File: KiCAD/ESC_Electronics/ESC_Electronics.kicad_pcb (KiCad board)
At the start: 2 copper layers, 149.5 x 74.5 mm, 70 parts, among them J1 -1000VDC, J2 Test Input, J3 CA probe, J4 DC Power, J5 Output, J6 Barrel_Jack, J7 -6V, J8 +6V, J9 Batt probe, Q1 MMBT3906, Q2 MMBT3904, U1 CR110, U2 SiPhotodiode, U3 TL072, U4 LM317, U5 TLE2426xP

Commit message: published as V2 on OSHPark
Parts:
- removed D3, D4: RB751V-40, Diode_SMD:D_SOD-323_HandSoldering
- removed D5, D6: MM3Z7V5T1G, Diode_SMD:D_SOD-323_HandSoldering
- removed Q1: MMBT3906, Package_TO_SOT_SMD:SOT-23
- removed Q2: MMBT3904, Package_TO_SOT_SMD:SOT-23
- removed R15: 220, Resistor_SMD:R_0805_2012Metric_Pad1.20x1.40mm_HandSolder
- removed R16, R17: 1k, Resistor_SMD:R_0805_2012Metric_Pad1.20x1.40mm_HandSolder
- removed R18, R19: 20, Resistor_SMD:R_1206_3216Metric_Pad1.30x1.75mm_HandSolder
- removed R20: 10k, Resistor_THT:R_Axial_DIN0207_L6.3mm_D2.5mm_P10.16mm_Horizontal
- removed R5: 100M, Resistor_THT:R_Axial_DIN0207_L6.3mm_D2.5mm_P10.16mm_Horizontal
- added C14: 0.33uF, Capacitor_SMD:C_0805_2012Metric_Pad1.18x1.45mm_HandSolder, F.Cu at (106.0, 106.5)
- added C15: 100nF, Capacitor_SMD:C_0805_2012Metric_Pad1.18x1.45mm_HandSolder, F.Cu at (100.7, 124.9)
- added C16: 100nF, Capacitor_SMD:C_0805_2012Metric_Pad1.18x1.45mm_HandSolder, F.Cu at (100.7, 119.8)
- added C17: 0.1uF, Capacitor_SMD:C_0805_2012Metric_Pad1.18x1.45mm_HandSolder, F.Cu at (70.5, 101.5)
- added C18: 0.1uF, Capacitor_SMD:C_0805_2012Metric_Pad1.18x1.45mm_HandSolder, F.Cu at (89.2, 101.5)
- added FB1: FerriteBead_Small, Inductor_SMD:L_1206_3216Metric_Pad1.22x1.90mm_HandSolder, F.Cu at (92.0, 86.8)
- added FB2: FerriteBead_Small, Inductor_SMD:L_1206_3216Metric_Pad1.22x1.90mm_HandSolder, F.Cu at (92.0, 80.6)
- added J10: RV Prob, Connector_PinHeader_2.54mm:PinHeader_1x02_P2.54mm_Vertical, F.Cu at (64.0, 96.0)
- added RV1: 10k, Potentiometer_THT:Potentiometer_Bourns_3266W_Vertical, F.Cu at (59.4, 88.3)
- added U6: UA79M08, Package_TO_SOT_SMD:TO-252-3_TabPin2, F.Cu at (97.6, 105.2)
- added U7: TLE2426xP, Package_SO:SOIC-8_3.9x4.9mm_P1.27mm, F.Cu at (106.6, 122.1)
- C10: value 1uF -> 0.1uF
- C11, C12: value 10uF -> 1uF
- C13: value 0.1uF -> 0.33uF
- C3: footprint Capacitor_THT:C_Disc_D10.5mm_W5.0mm_P7.50mm -> Capacitor_THT:C_Disc_D10.5mm_W5.0mm_P10.00mm
- C5: value 1nF -> 1pF; footprint Capacitor_THT:C_Disc_D10.5mm_W5.0mm_P7.50mm -> Capacitor_THT:C_Disc_D7.5mm_W5.0mm_P5.00mm
- C6: value 1pF -> 4700pF; footprint Capacitor_THT:C_Disc_D7.5mm_W5.0mm_P5.00mm -> Capacitor_THT:C_Disc_D12.5mm_W5.0mm_P10.00mm
- C7: value 4700pF -> 1nF; footprint Capacitor_THT:C_Disc_D14.5mm_W5.0mm_P7.50mm -> Capacitor_THT:C_Disc_D10.5mm_W5.0mm_P10.00mm
- C8: value 1uF -> open
- J1: value -1000VDC -> Batt probe; footprint ESC_Electronics_Library:MHV Wire Conn -> Connector_PinHeader_2.54mm:PinHeader_1x02_P2.54mm_Vertical
- J2: value Test Input -> CA probe; footprint Connector_Coaxial:BNC_Amphenol_B6252HB-NPP3G-50_Horizontal -> Connector_PinHeader_2.54mm:PinHeader_1x02_P2.54mm_Vertical
- J3: value CA probe -> Test Input; footprint Connector_PinHeader_2.54mm:PinHeader_1x02_P2.54mm_Vertical -> Connector_Coaxial:BNC_Amphenol_B6252HB-NPP3G-50_Horizontal
- J4: value DC Power -> -1000VDC; footprint TerminalBlock_4Ucon:TerminalBlock_4Ucon_1x03_P3.50mm_Vertical -> ESC_Electronics_Library:MHV Wire Conn
- J6: footprint Connector_Wire:SolderWire-0.5sqmm_1x02_P4.6mm_D0.9mm_OD2.1mm -> Connector_PinHeader_2.54mm:PinHeader_1x02_P2.54mm_Vertical
- J7: value -6V -> DC Power; footprint Connector_PinHeader_2.54mm:PinHeader_1x02_P2.54mm_Vertical -> Connector_PinHeader_2.54mm:PinHeader_1x03_P2.54mm_Vertical
- J8: value +6V -> -8V
- J9: value Batt probe -> +8V
- R10: value 47 -> 750
- R11: value 1k -> 20k; footprint Resistor_THT:R_Axial_DIN0207_L6.3mm_D2.5mm_P10.16mm_Horizontal -> Resistor_SMD:R_0805_2012Metric_Pad1.20x1.40mm_HandSolder
- R12: value 10k -> 4.7; footprint Resistor_THT:R_Axial_DIN0207_L6.3mm_D2.5mm_P10.16mm_Horizontal -> Resistor_SMD:R_2512_6332Metric_Pad1.40x3.35mm_HandSolder
- R13: value 4.7 -> 7k; footprint Resistor_SMD:R_2512_6332Metric_Pad1.40x3.35mm_HandSolder -> Resistor_SMD:R_0805_2012Metric_Pad1.20x1.40mm_HandSolder
- R14: value 2.94k -> 470
- R2: value 4.7 -> 10M; footprint Resistor_SMD:R_2512_6332Metric_Pad1.40x3.35mm_HandSolder -> Resistor_THT:R_Axial_DIN0207_L6.3mm_D2.5mm_P15.24mm_Horizontal
- R3: footprint Resistor_THT:R_Axial_DIN0207_L6.3mm_D2.5mm_P10.16mm_Horizontal -> Resistor_THT:R_Axial_DIN0207_L6.3mm_D2.5mm_P15.24mm_Horizontal
- R4: value 10M -> 100M; footprint Resistor_THT:R_Axial_DIN0207_L6.3mm_D2.5mm_P10.16mm_Horizontal -> Resistor_THT:R_Axial_DIN0207_L6.3mm_D2.5mm_P15.24mm_Horizontal
- R6: value 0 -> 10M; footprint Resistor_THT:R_Axial_DIN0207_L6.3mm_D2.5mm_P10.16mm_Horizontal -> Resistor_THT:R_Axial_DIN0207_L6.3mm_D2.5mm_P15.24mm_Horizontal
- R7: value 4.7 -> 47; footprint Resistor_SMD:R_2512_6332Metric_Pad1.40x3.35mm_HandSolder -> Resistor_SMD:R_0805_2012Metric_Pad1.20x1.40mm_HandSolder
- R8: value 10M -> open; footprint Resistor_THT:R_Axial_DIN0207_L6.3mm_D2.5mm_P10.16mm_Horizontal -> Resistor_THT:R_Axial_DIN0207_L6.3mm_D2.5mm_P15.24mm_Horizontal
- R9: value open -> 0; footprint Resistor_THT:R_Axial_DIN0207_L6.3mm_D2.5mm_P7.62mm_Horizontal -> Resistor_SMD:R_1206_3216Metric_Pad1.30x1.75mm_HandSolder
- U3: value TL072 -> TL051CP
- U4: value LM317 -> LM317L; footprint Package_TO_SOT_THT:TO-220-3_Horizontal_TabDown -> Package_TO_SOT_SMD:SOT-89-3_Handsoldering
- U5: value TLE2426xP -> UA78M08; footprint Package_TO_SOT_THT:TO-92L_Inline_Wide -> Package_TO_SOT_SMD:SOT-223-3_TabPin2
- moved J4 111.6 mm to (164.8, 63.8), turned to 0 degrees
- moved R9 102.6 mm to (84.7, 90.8), turned to 180 degrees
- moved C6 73.1 mm to (137.8, 71.8), turned to 180 degrees
- moved J9 70.2 mm to (79.0, 97.8)
- moved R2 66.0 mm to (138.8, 111.4)
- moved J1 62.8 mm to (127.0, 108.8), turned to 180 degrees
- moved C5 60.8 mm to (119.0, 64.5), turned to 90 degrees
- moved C7 55.0 mm to (188.5, 61.8), turned to -90 degrees
- moved J5 46.5 mm to (60.7, 65.2)
- moved R7 42.6 mm to (113.5, 63.8)
- moved R12 40.7 mm to (78.0, 124.8), turned to 180 degrees
- moved C9 40.6 mm to (70.6, 75.2), turned to 90 degrees
- moved C10 37.8 mm to (54.8, 82.8), turned to 90 degrees
- moved C2 37.8 mm to (90.8, 66.2), turned to 90 degrees
- moved R4 35.8 mm to (148.9, 72.0), turned to 0 degrees
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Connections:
- C1 pad 1: +6VDC -> Net-(C1-Pad1)
- C10 pad 1: Net-(C10-Pad1) -> +8VDC
- C10 pad 2: Net-(C10-Pad2) -> GND
- C11 pad 2: GND -> Net-(C11-Pad2)
- C12 pad 2: GND -> Net-(C11-Pad2)
- C13 pad 1: -6VDC -> Net-(C13-Pad1)
- C3 pad 2: Net-(C3-Pad2) -> Net-(R2-Pad2)
- C4 pad 1: -6VDC -> Net-(C4-Pad1)
- C5 pad 1: GND -> Net-(C2-Pad1)
- C5 pad 2: Net-(R5-Pad2) -> Net-(C5-Pad2)
- C6 pad 1: Net-(C2-Pad1) -> Net-(BT1-Pad2)
- C6 pad 2: Net-(C6-Pad2) -> GND
- C7 pad 1: Net-(BT1-Pad2) -> GND
- C7 pad 2: GND -> Net-(C7-Pad2)
- C8 pad 2: Net-(C10-Pad2) -> GND
- C9 pad 1: +6VDC -> -8VDC
- D1 pad 1: Net-(D1-Pad1) -> Net-(C13-Pad1)
- D1 pad 2: Net-(D1-Pad2) -> Net-(C12-Pad1)
- D2 pad 1: Net-(D2-Pad1) -> Net-(C11-Pad2)
- D2 pad 2: Net-(D2-Pad2) -> Net-(C14-Pad1)
- J1 pad 1: Net-(J1-Pad1) -> Net-(BT6-Pad1)
- J1 pad 2: GND -> Net-(BT1-Pad2)
- J2 pad 1: Net-(C6-Pad2) -> GND
- J2 pad 2: GND -> Net-(J2-Pad2)
- J3 pad 1: Net-(J3-Pad1) -> Net-(C5-Pad2)
- J4 pad 1: Net-(D2-Pad1) -> Net-(J4-Pad1)
- J6 pad 2: Net-(C10-Pad2) -> Net-(C11-Pad2)
- J7 pad 1: -6VDC -> Net-(C14-Pad1)
- J8 pad 1: +6VDC -> -8VDC
- J9 pad 1: Net-(BT6-Pad1) -> +8VDC
- J9 pad 2: Net-(BT1-Pad2) -> GND
- R10 pad 1: Net-(C6-Pad2) -> Net-(R10-Pad1)
- R10 pad 2: GND -> Net-(R10-Pad2)
- R11 pad 1: Net-(J3-Pad1) -> Net-(R10-Pad2)
- R11 pad 2: Net-(R11-Pad2) -> Net-(J5-Pad1)
- R12 pad 1: GND -> Net-(C11-Pad1)
- R12 pad 2: Net-(R12-Pad2) -> Net-(L1-Pad2)
- R13 pad 1: Net-(C8-Pad1) -> Net-(R13-Pad1)
- R13 pad 2: Net-(L1-Pad2) -> Net-(C11-Pad2)
- R14 pad 1: Net-(R14-Pad1) -> Net-(C12-Pad1)
- R14 pad 2: Net-(C10-Pad2) -> Net-(R13-Pad1)
- R2 pad 1: +6VDC -> Net-(R2-Pad1)
- R3 pad 1: Net-(R3-Pad1) -> Net-(BT6-Pad1)
- R3 pad 2: Net-(R3-Pad2) -> Net-(R2-Pad1)
- R4 pad 1: Net-(BT6-Pad1) -> Net-(R2-Pad2)
- R4 pad 2: Net-(R3-Pad1) -> Net-(C7-Pad2)
- R6 pad 1: Net-(C3-Pad2) -> Net-(C7-Pad2)
- R6 pad 2: Net-(R3-Pad2) -> Net-(J4-Pad1)
- R7 pad 1: -6VDC -> Net-(C5-Pad2)
- R7 pad 2: Net-(R7-Pad2) -> GND
- R8 pad 1: Net-(R5-Pad2) -> Net-(R2-Pad2)
- R8 pad 2: Net-(J1-Pad1) -> GND
- R9 pad 1: Net-(R3-Pad2) -> Net-(J2-Pad2)
- R9 pad 2: GND -> Net-(C8-Pad1)
- U1 pad 5: Net-(R7-Pad2) -> Net-(C4-Pad1)
- U1 pad 6: Net-(R2-Pad2) -> Net-(C1-Pad1)
- U1 pad 8: Net-(J3-Pad1) -> Net-(J2-Pad2)
- U2 pad 2: Net-(R3-Pad2) -> Net-(R2-Pad2)
- U3 pad 2: Net-(R12-Pad2) -> Net-(R10-Pad2)
- U3 pad 3: Net-(R11-Pad2) -> Net-(C8-Pad1)
- U3 pad 4: -6VDC -> -8VDC
- U3 pad 8: +6VDC -> +8VDC
- U4 pad 1: Net-(R14-Pad1) -> Net-(R13-Pad1)
- U4 pad 2: Net-(C10-Pad1) -> Net-(C12-Pad1)
- U4 pad 3: Net-(C8-Pad1) -> Net-(C11-Pad1)
- U5 pad 1: GND -> Net-(C13-Pad1)
- U5 pad 2: Net-(C10-Pad2) -> GND
- U5 pad 3: Net-(C10-Pad1) -> +8VDC
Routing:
- net GND: track 21.3 -> 145.5 mm, vias 9 -> 27
- net Net-(R3-Pad2): track 91.5 -> 0.00 mm
- net Net-(C11-Pad2): track 0.00 -> 81.9 mm
- net -6VDC: track 74.9 -> 0.00 mm, vias 2 -> 0
- net +8VDC: track 0.00 -> 69.6 mm, vias 0 -> 1
- net -8VDC: track 0.00 -> 67.9 mm, vias 0 -> 1
- net +6VDC: track 57.1 -> 0.00 mm
- net Net-(C10-Pad2): track 54.4 -> 0.00 mm
- net Net-(C12-Pad1): track 13.0 -> 53.3 mm, vias 0 -> 4
- net Net-(C2-Pad1): track 87.8 -> 48.4 mm
- net Net-(C10-Pad1): track 33.0 -> 0.00 mm
- net Net-(R2-Pad2): track 11.4 -> 44.0 mm
- net Net-(J2-Pad2): track 0.00 -> 31.4 mm
- net Net-(C14-Pad1): track 0.00 -> 30.2 mm, vias 0 -> 1
- net Net-(C13-Pad1): track 0.00 -> 28.4 mm
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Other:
- board text added: "+ Batt -"
- board text added: "+10V GND -10V"
- board text added: "+8V GND"
- board text added: "-8V GND"
- board text added: "0-10kOhm"
- board text added: "4.7Ohm"
- board text added: "<P1"
- board text added: "A = 1+20k/(.75+RV) RV=0, A=~27 RV=10, A=~3"
- board text added: "RV Probe"
- board text added: "SiPM"
- board text added: "Test"
- board text removed: "+6V GND"
- board text removed: "+8V GND -8V"
- board text removed: "-6V GND"
- board text removed: "0 Ohm"
- board text removed: "1pF"
- board text removed: "1uF"
- board text removed: "A = 1+R20/R12"
- board text removed: "Batt +"
- board text removed: "DIODE"
- board text removed: "HV"
- board text removed: "Input Only"
- board text removed: "TL072"
- board text removed: "Test Input"

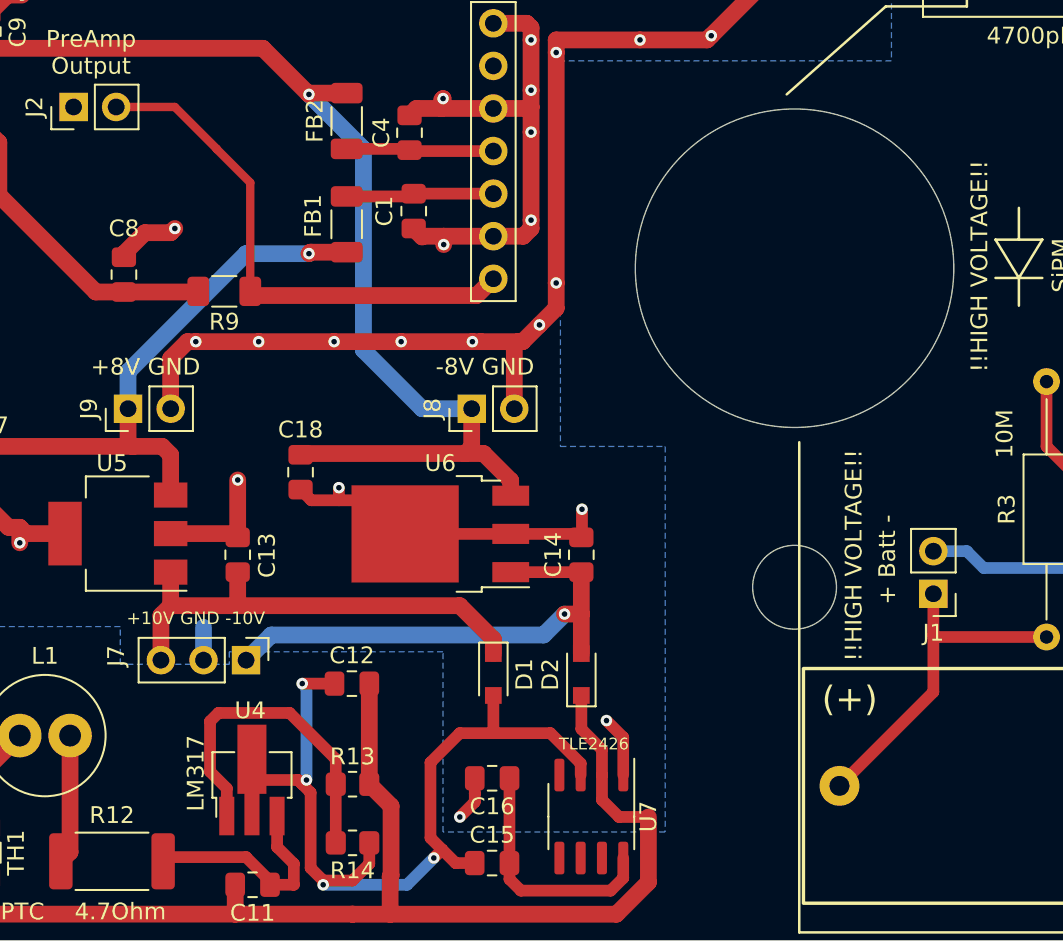
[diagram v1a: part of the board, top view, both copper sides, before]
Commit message: fixed U6 pad and updated several footprints to latest KiCAD versions
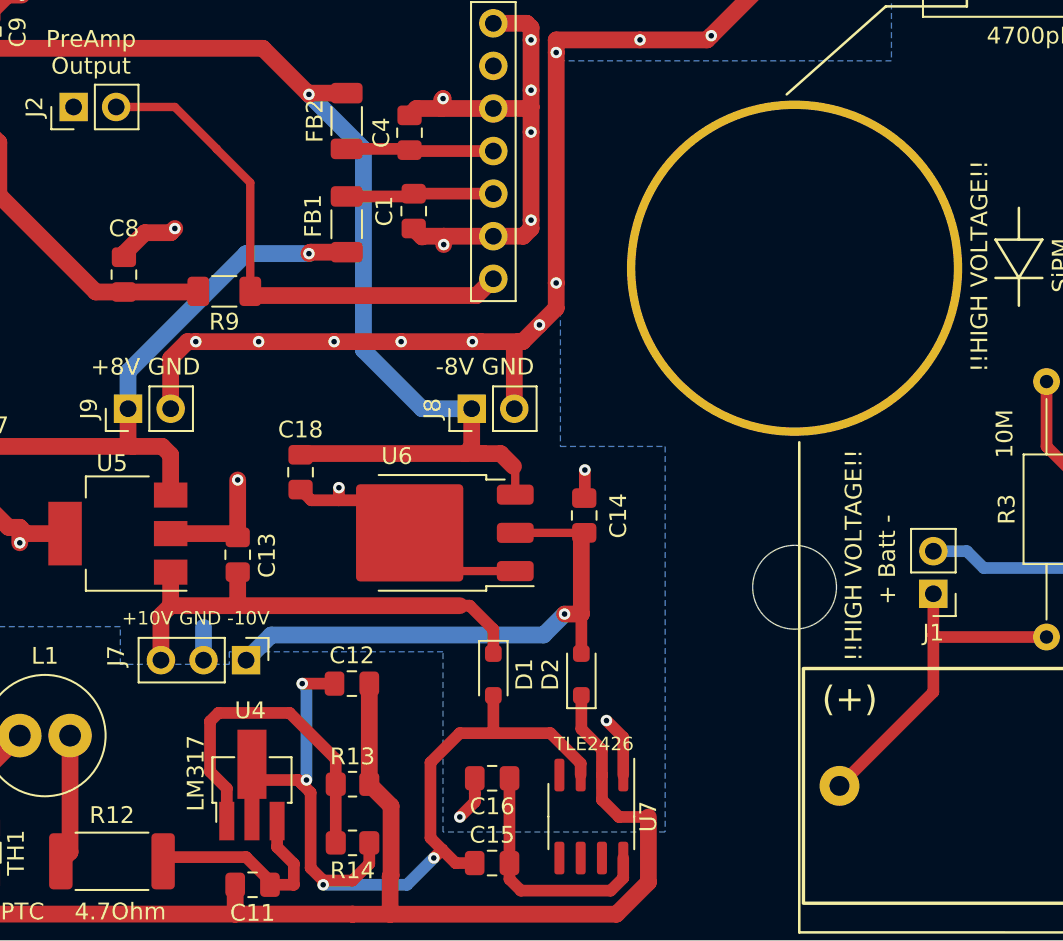
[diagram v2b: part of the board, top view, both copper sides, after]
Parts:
- U6: footprint Package_TO_SOT_SMD:TO-252-3_TabPin2 -> ESC_Electronics_Library:TO-252-3_Tab1
- moved C14 2.35 mm to (106.2, 104.1)
- moved U6 0.57 mm to (97.0, 105.2)
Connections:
- C14 pad 1: Net-(C14-Pad1) -> Net-(D2-A)
- D2 pad 2: Net-(C14-Pad1) -> Net-(D2-A)
- J7 pad 1: Net-(C14-Pad1) -> Net-(D2-A)
- U6 pad 1: Net-(C14-Pad1) -> GND
- U6 pad 2: GND -> Net-(D2-A)
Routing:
- net Net-(D2-A): track 0.00 -> 32.3 mm, vias 0 -> 1
- net Net-(C14-Pad1): track 30.2 -> 0.00 mm, vias 1 -> 0
- net GND: track 145.5 -> 144.0 mm
- net -8VDC: track 67.9 -> 68.6 mm

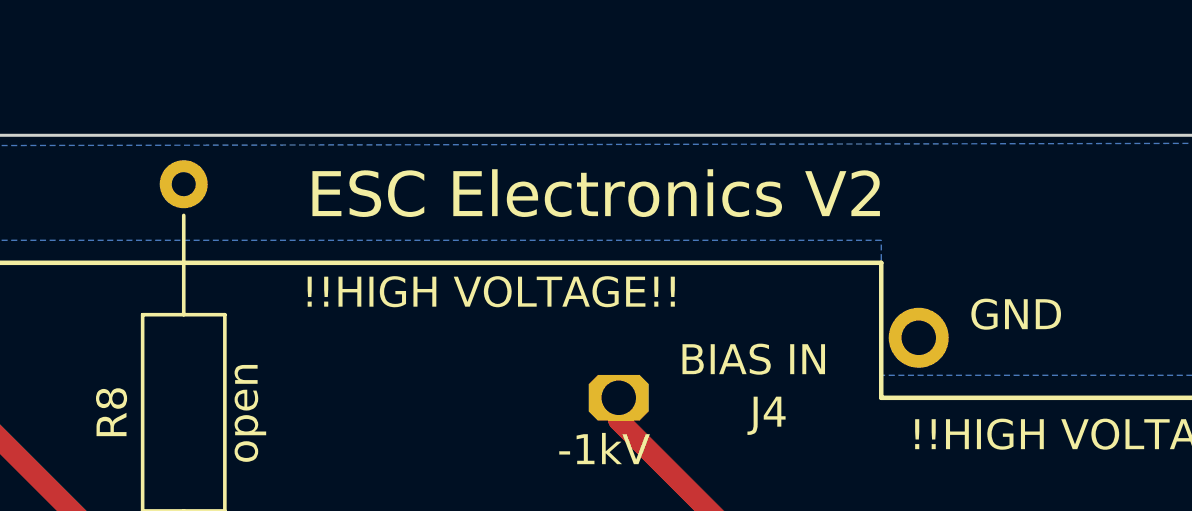
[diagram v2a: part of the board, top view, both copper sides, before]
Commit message: Updated PDB label to V2b for #4 fix
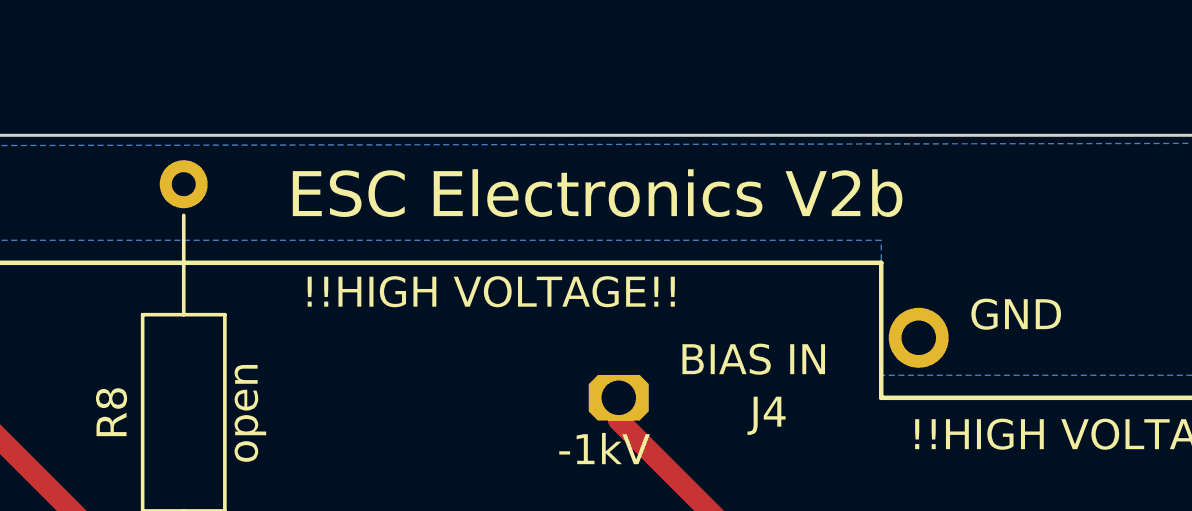
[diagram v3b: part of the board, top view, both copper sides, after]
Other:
- board text added: "ESC Electronics V2b"
- board text removed: "ESC Electronics V2"
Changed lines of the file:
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@@
     (effects (font (size 1.5 1.5) (thickness 0.3)))
   )
-  (gr_text "ESC Electronics V2" (at 159 57) (layer "F.SilkS")
+  (gr_text "ESC Electronics V2b" (at 159 57) (layer "F.SilkS")
     (effects (font (size 1.5 1.5) (thickness 0.2)))
   )

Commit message: Cleaning up SCH w/ notes
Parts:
- J3: value Test Input -> Test Input BNC
- J4: value -1000VDC -> -1000VDC SHV
- J5: value Output -> Output BNC
- J6: value Barrel_Jack -> Wire
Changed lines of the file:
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@@
   (net 11 "Net-(U2-N)")
   (net 12 "Net-(U1--Vs)")
-  (net 13 "Net-(J6-Pad1)")
+  (net 13 "Net-(J6-Pin_1)")
   (net 14 "Net-(L1-Pad2)")
   (net 15 "Net-(J3-In)")
@@
     (descr "Resistor, Axial_DIN0207 series, Axial, Horizontal, pin pitch=15.24mm, 0.25W = 1/4W, length*diameter=6.3*2.5mm^2, http://cdn-reichelt.de/documents/datenblatt/B400/1_4W%23YAG.pdf")
     (tags "Resistor Axial_DIN0207 series Axial Horizontal pin pitch 15.24mm 0.25W = 1/4W length 6.3mm diameter 2.5mm")
-    (property "Digikey" "HVA05FA10M0CT-ND")
+    (property "Digikey" "HVA12FA10M0")
     (property "Sheetfile" "ESC_Electronics.kicad_sch")
     (property "Sheetname" "")
@@
     (descr "Through hole straight pin header, 1x02, 2.54mm pitch, single row")
     (tags "Through hole pin header THT 1x02 2.54mm single row")
+    (property "Digikey" "N/A")
     (property "Sheetfile" "ESC_Electronics.kicad_sch")
     (property "Sheetname" "")
@@
     (descr "Resistor, Axial_DIN0207 series, Axial, Horizontal, pin pitch=15.24mm, 0.25W = 1/4W, length*diameter=6.3*2.5mm^2, http://cdn-reichelt.de/documents/datenblatt/B400/1_4W%23YAG.pdf")
     (tags "Resistor Axial_DIN0207 series Axial Horizontal pin pitch 15.24mm 0.25W = 1/4W length 6.3mm diameter 2.5mm")
-    (property "Digikey" "HVA05FA100MCT-ND ")
+    (property "Digikey" "HVA12FA100MCT-ND")
     (property "Sheetfile" "ESC_Electronics.kicad_sch")
     (property "Sheetname" "")
@@
         (effects (font (size 1 1) (thickness 0.15)))
     )
-    (fp_text value "Output" (at 12.455 12.92 90) (layer "F.Fab")
+    (fp_text value "Output BNC" (at 12.455 12.92 90) (layer "F.Fab")
         (effects (font (size 1 1) (thickness 0.15)))
     )
@@
     (descr "Through hole straight pin header, 1x03, 2.54mm pitch, single row")
     (tags "Through hole pin header THT 1x03 2.54mm single row")
+    (property "Digikey" "N/A")
     (property "Sheetfile" "ESC_Electronics.kicad_sch")
     (property "Sheetname" "")
@@
       (net 22 "Net-(L1-Pad1)") (pintype "passive"))
     (pad "2" smd roundrect (at 1.4875 0 270) (size 1.425 2.65) (layers "F.Cu" "F.Paste" "F.Mask") (roundrect_rratio 0.175439)
-      (net 13 "Net-(J6-Pad1)") (pintype "passive"))
+      (net 13 "Net-(J6-Pin_1)") (pintype "passive"))
     (model "${KICAD6_3DMODEL_DIR}/Fuse.3dshapes/Fuse_1210_3225Metric.wrl"
       (offset (xyz 0 0 0))
@@
   (footprint "ESC_Electronics_Library:MHV Wire Conn" (layer "F.Cu")
     (at 164.75 63.75)
-    (property "Digikey" "2737-RHV-116-ND")
+    (property "Digikey" "4912-SHV-BR-ND")
     (property "Sheetfile" "ESC_Electronics.kicad_sch")
     (property "Sheetname" "")
@@
         (effects (font (size 1 1) (thickness 0.15)))
     )
-    (fp_text value "-1000VDC" (at 0 -2.54 unlocked) (layer "F.Fab")
+    (fp_text value "-1000VDC SHV" (at 0 -2.54 unlocked) (layer "F.Fab")
         (effects (font (size 1 1) (thickness 0.15)))
     )
@@
     (descr "Through hole straight pin header, 1x02, 2.54mm pitch, single row")
     (tags "Through hole pin header THT 1x02 2.54mm single row")
-    (property "Digikey" "839-1580-ND")
+    (property "Digikey" "")
     (property "Sheetfile" "ESC_Electronics.kicad_sch")
     (property "Sheetname" "")
-    (property "ki_description" "DC Barrel Jack")
-    (property "ki_keywords" "DC power barrel jack connector")
+    (property "ki_description" "Generic connector, single row, 01x02, script generated")
+    (property "ki_keywords" "connector")
     (attr through_hole)
     (fp_text reference "J6" (at 2.75 1 180) (layer "F.SilkS")
         (effects (font (size 1 1) (thickness 0.15)))
     )
-    (fp_text value "Barrel_Jack" (at 0 4.87 90) (layer "F.Fab")
+    (fp_text value "Wire" (at 0 4.87 90) (layer "F.Fab")
         (effects (font (size 1 1) (thickness 0.15)))
     )
@@
       (stroke (width 0.1) (type solid)) (layer "F.Fab"))
     (pad "1" thru_hole rect (at 0 0 270) (size 1.7 1.7) (drill 1) (layers "*.Cu" "*.Mask")
-      (net 13 "Net-(J6-Pad1)") (pintype "power_out"))
+      (net 13 "Net-(J6-Pin_1)") (pinfunction "Pin_1") (pintype "passive"))
     (pad "2" thru_hole oval (at 0 2.54 270) (size 1.7 1.7) (drill 1) (layers "*.Cu" "*.Mask")
-      (net 18 "Net-(D2-K)") (pintype "power_out"))
+      (net 18 "Net-(D2-K)") (pinfunction "Pin_2") (pintype "passive"))
     (model "${KICAD6_3DMODEL_DIR}/Connector_PinHeader_2.54mm.3dshapes/PinHeader_1x02_P2.54mm_Vertical.wrl"
       (offset (xyz 0 0 0))
@@
     (descr "Through hole straight pin header, 1x02, 2.54mm pitch, single row")
     (tags "Through hole pin header THT 1x02 2.54mm single row")
+    (property "Digikey" "N/A")
     (property "Sheetfile" "ESC_Electronics.kicad_sch")
     (property "Sheetname" "")
@@
     (descr "Potentiometer, vertical, Bourns 3266W, https://www.bourns.com/docs/Product-Datasheets/3266.pdf")
     (tags "Potentiometer vertical Bourns 3266W")
+    (property "Digikey" "3266W-103LF-ND")
     (property "Sheetfile" "ESC_Electronics.kicad_sch")
     (property "Sheetname" "")
@@
     (descr "Resistor SMD 1206 (3216 Metric), square (rectangular) end terminal, IPC_7351 nominal with elongated pad for handsoldering. (Body size source: IPC-SM-782 page 72, https://www.pcb-3d.com/wordpress/wp-content/uploads/ipc-sm-782a_amendment_1_and_2.pdf), generated with kicad-footprint-generator")
     (tags "resistor handsolder")
-    (property "Digikey" "RNCP0805FTD1K00CT-ND")
+    (property "Digikey" "RMCF0805ZT0R00")
     (property "Sheetfile" "ESC_Electronics.kicad_sch")
     (property "Sheetname" "")
@@
         (effects (font (size 1 1) (thickness 0.15)))
     )
-    (fp_text value "Test Input" (at 0 6 180) (layer "F.Fab")
+    (fp_text value "Test Input BNC" (at 0 6 180) (layer "F.Fab")
         (effects (font (size 1 1) (thickness 0.15)))
     )
@@
     (descr "Through hole straight pin header, 1x08, 2.54mm pitch, single row")
     (tags "Through hole pin header THT 1x08 2.54mm single row")
+    (property "Digikey" "ED11161-ND")
     (property "Sheetfile" "ESC_Electronics.kicad_sch")
     (property "Sheetname" "")
@@
     (descr "Resistor, Axial_DIN0207 series, Axial, Horizontal, pin pitch=15.24mm, 0.25W = 1/4W, length*diameter=6.3*2.5mm^2, http://cdn-reichelt.de/documents/datenblatt/B400/1_4W%23YAG.pdf")
     (tags "Resistor Axial_DIN0207 series Axial Horizontal pin pitch 15.24mm 0.25W = 1/4W length 6.3mm diameter 2.5mm")
-    (property "Digikey" "HVA05FA10M0CT-ND")
+    (property "Digikey" "HVA12FA10M0CT-ND")
     (property "Sheetfile" "ESC_Electronics.kicad_sch")
     (property "Sheetname" "")
@@
     (descr "Resistor, Axial_DIN0207 series, Axial, Horizontal, pin pitch=15.24mm, 0.25W = 1/4W, length*diameter=6.3*2.5mm^2, http://cdn-reichelt.de/documents/datenblatt/B400/1_4W%23YAG.pdf")
     (tags "Resistor Axial_DIN0207 series Axial Horizontal pin pitch 15.24mm 0.25W = 1/4W length 6.3mm diameter 2.5mm")
-    (property "Digikey" "HVA05FA10M0CT-ND")
+    (property "Digikey" "HVA12FA10M0CT-ND")
     (property "Sheetfile" "ESC_Electronics.kicad_sch")
     (property "Sheetname" "")
